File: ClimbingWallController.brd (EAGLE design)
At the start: 100 x 80 mm, 339 parts, among them IC1 74HCT138D, IC2 SN74LV4052AD, IC3 PIC24FJ32GB004, IC4 TLC5952, IC5 TLC5952, IC6 TC1015, IC8 74HCT138D, IC9 SN74LV4052AD, J1 PWR, Q1 DPBT8105, Q10 DPBT8105, Q11 DPBT8105, Q12 DPBT8105, Q13 DPBT8105, Q14 DPBT8105, Q15 DPBT8105, Q16 DPBT8105, Q17 DPBT8105, Q2 DPBT8105, Q3 DPBT8105, Q4 DPBT8105, Q5 DPBT8105, Q6 DPBT8105, Q7 DPBT8105, Q8 DPBT8105, Q9 NC, X1 MINI-USB-32005-201

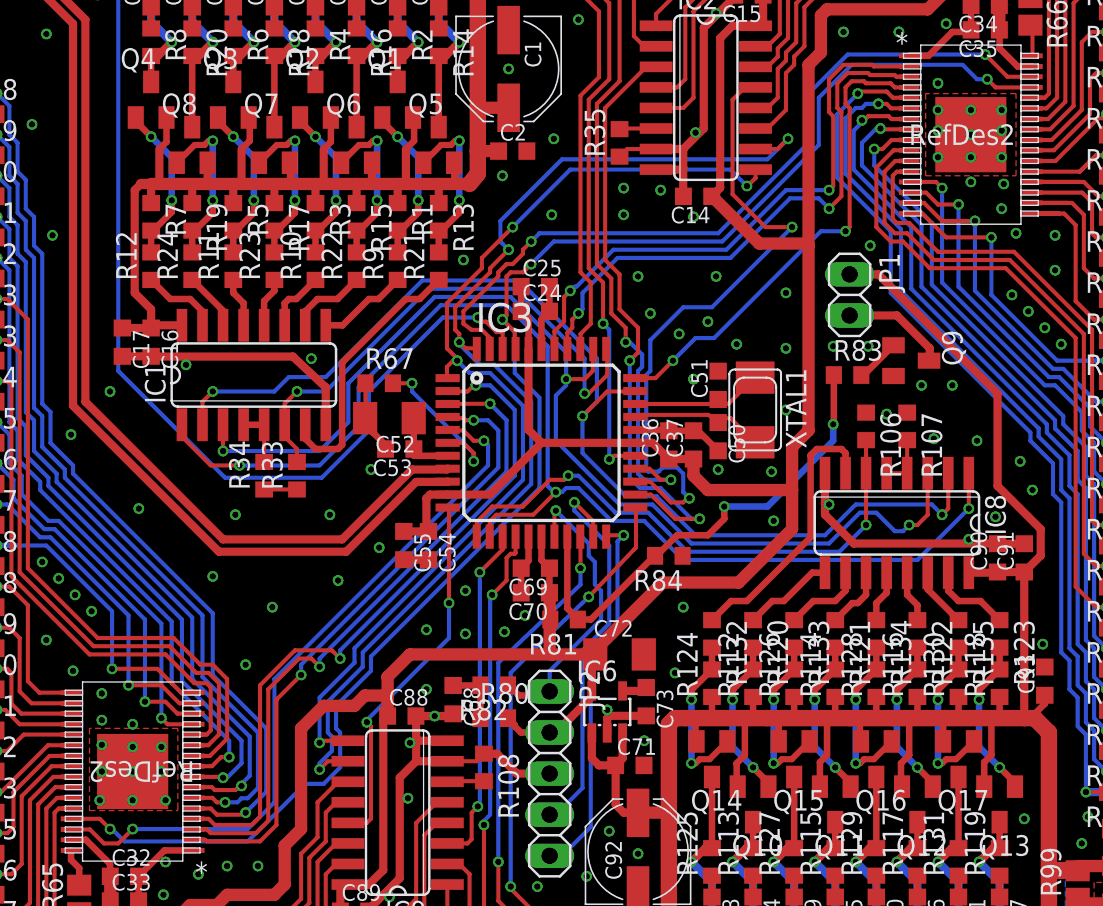
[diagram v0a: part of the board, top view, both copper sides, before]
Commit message: Optimized LED Driver footprint and paste mask to match the datasheet. Optimized a few signal routes to reduce noise coupling. Reviewed trace coupling on sensitive nodes. (Layout is good).
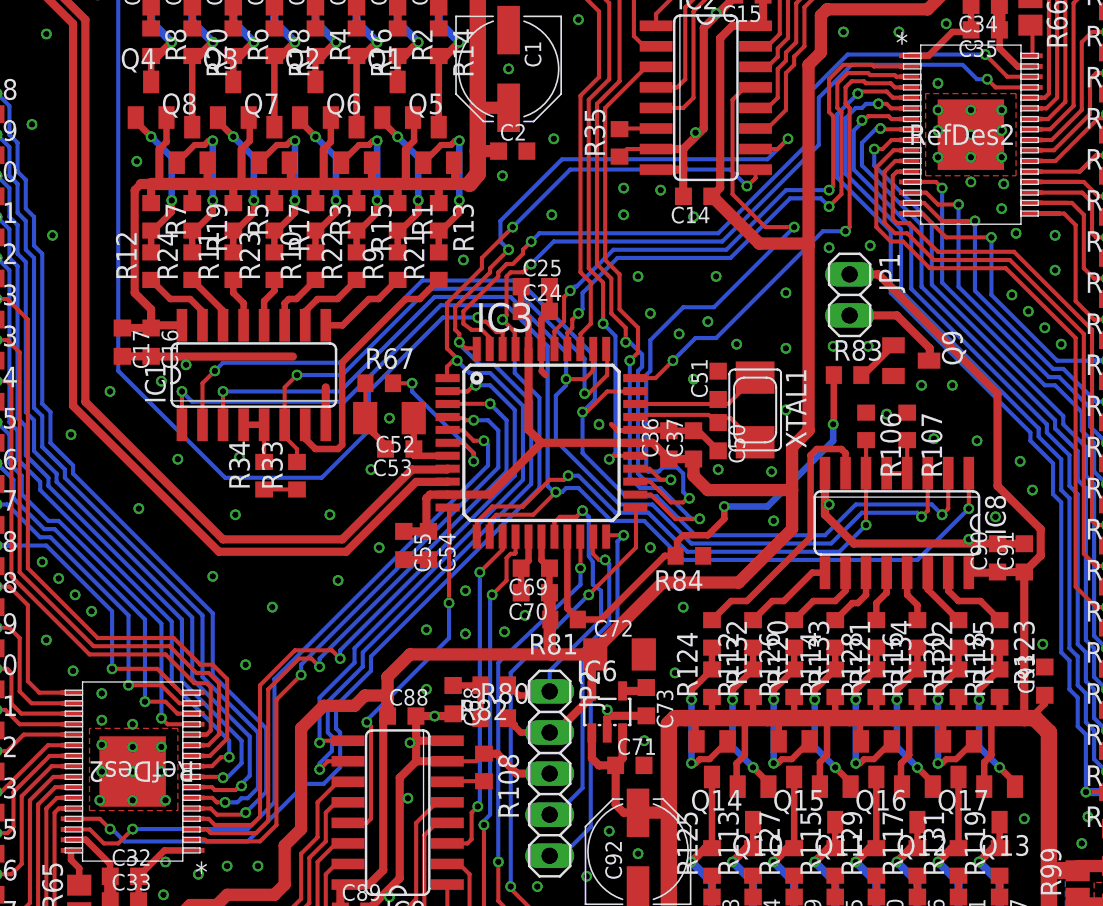
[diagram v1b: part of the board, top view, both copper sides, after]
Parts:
- moved R84 1.27 mm to (58.7, 33.7)
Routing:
- net PGED: track 24.6 -> 19.6 mm
- net RSEL2: track 69.0 -> 65.6 mm
- net RSEL0: track 76.7 -> 75.2 mm
- net MCLR_: track 18.2 -> 18.9 mm
- net RBEN: track 32.9 -> 33.4 mm
- net GND: track 345.3 -> 345.4 mm, vias 247 -> 254

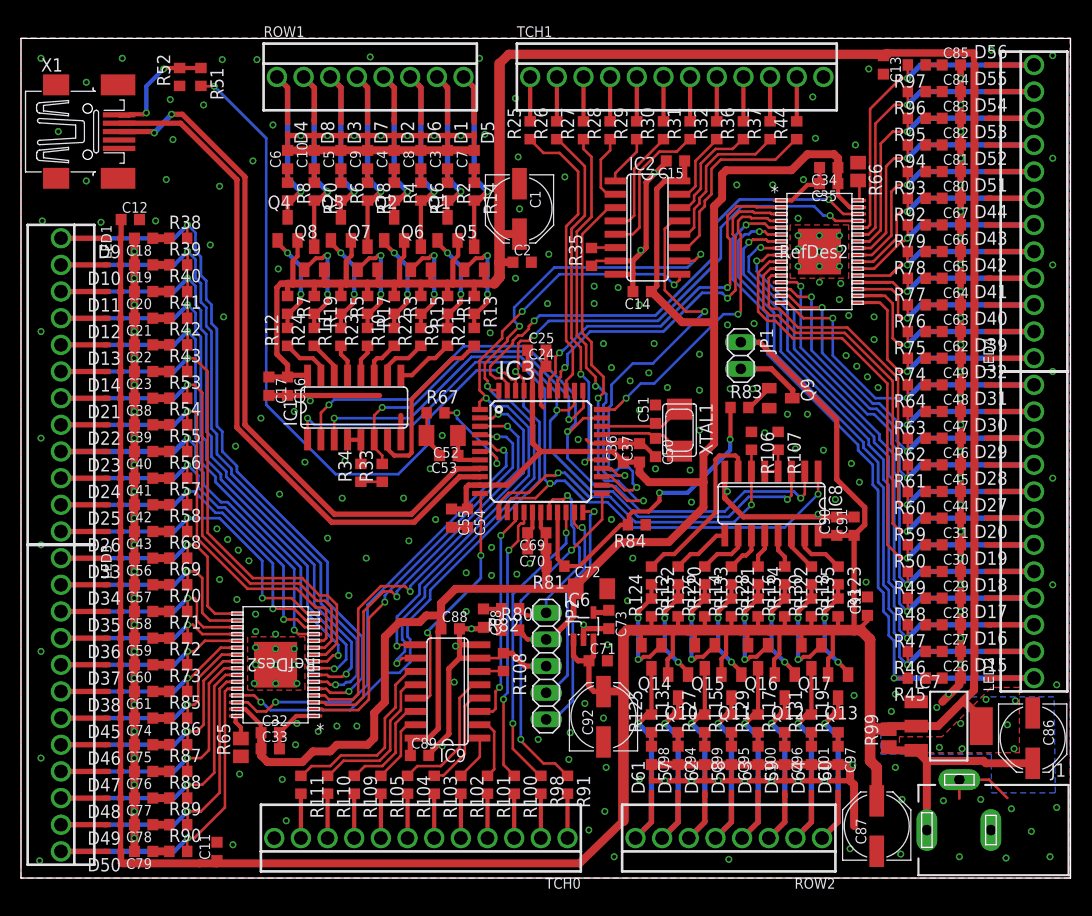
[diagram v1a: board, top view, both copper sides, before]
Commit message: Improved 5v power routing for etching concerns.
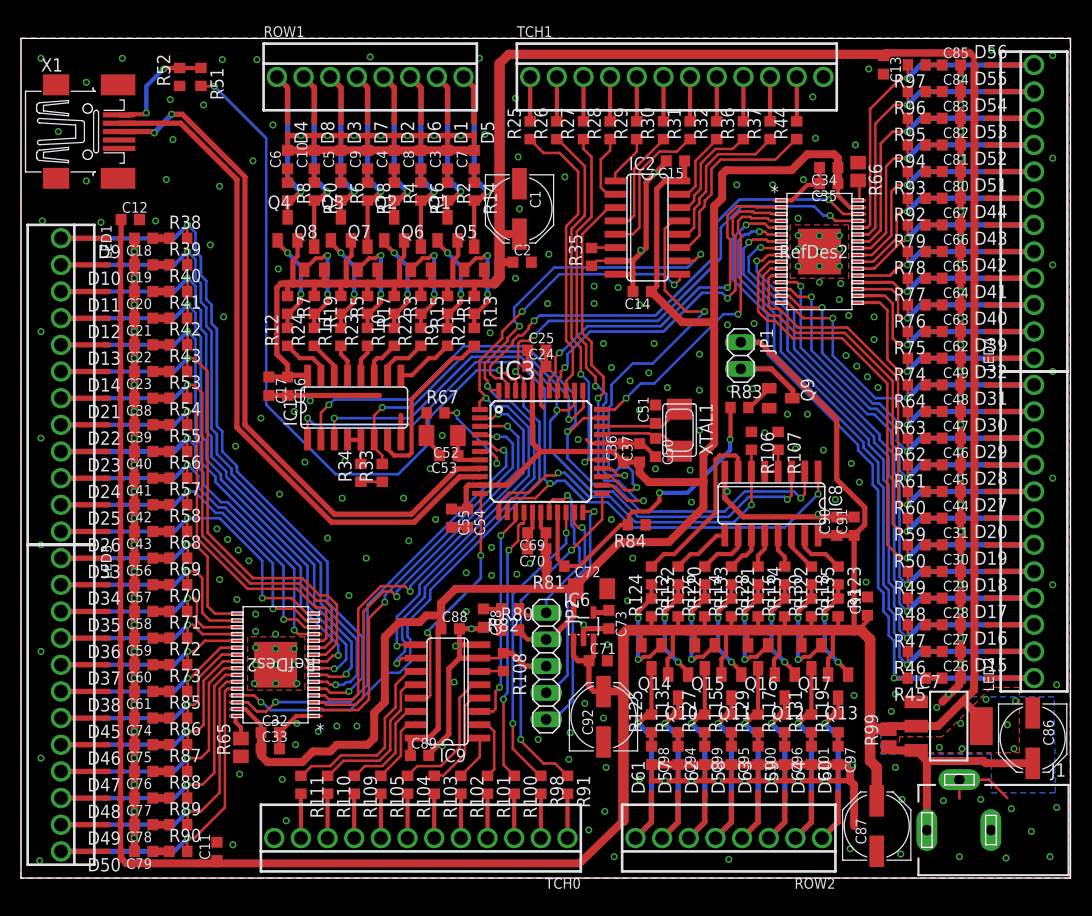
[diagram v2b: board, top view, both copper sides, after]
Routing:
- net +5V: track 491.3 -> 490.8 mm
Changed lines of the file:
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@@
 <setting verticaltext="up"/>
 </settings>
-<grid distance="0.05" unitdist="inch" unit="inch" style="lines" multiple="1" display="yes" altdistance="0.005" altunitdist="inch" altunit="inch"/>
+<grid distance="0.5" unitdist="mil" unit="mil" style="lines" multiple="1" display="yes" altdistance="0.005" altunitdist="inch" altunit="inch"/>
 <layers>
 <layer number="1" name="Top" color="4" fill="1" visible="yes" active="yes"/>
@@
 <layer number="25" name="tNames" color="7" fill="1" visible="yes" active="yes"/>
 <layer number="26" name="bNames" color="7" fill="1" visible="yes" active="yes"/>
-<layer number="27" name="tValues" color="7" fill="1" visible="no" active="yes"/>
-<layer number="28" name="bValues" color="7" fill="1" visible="no" active="yes"/>
+<layer number="27" name="tValues" color="7" fill="1" visible="yes" active="yes"/>
+<layer number="28" name="bValues" color="7" fill="1" visible="yes" active="yes"/>
 <layer number="29" name="tStop" color="7" fill="3" visible="yes" active="yes"/>
 <layer number="30" name="bStop" color="7" fill="6" visible="yes" active="yes"/>
@@
 <layer number="199" name="Contour" color="7" fill="1" visible="yes" active="yes"/>
 <layer number="200" name="200bmp" color="1" fill="10" visible="yes" active="yes"/>
-<layer number="201" name="201bmp" color="2" fill="1" visible="no" active="no"/>
-<layer number="202" name="202bmp" color="3" fill="1" visible="no" active="no"/>
+<layer number="201" name="201bmp" color="2" fill="10" visible="yes" active="yes"/>
+<layer number="202" name="202bmp" color="3" fill="10" visible="yes" active="yes"/>
 <layer number="203" name="203bmp" color="4" fill="10" visible="yes" active="yes"/>
 <layer number="204" name="204bmp" color="5" fill="10" visible="yes" active="yes"/>
@@
 <wire x1="57.404" y1="5.461" x2="53.213" y2="1.397" width="0.762" layer="1"/>
 <wire x1="53.213" y1="1.397" x2="17.018" y2="1.397" width="0.762" layer="1"/>
-<wire x1="17.018" y1="1.397" x2="9.652" y2="1.397" width="0.762" layer="1"/>
-<wire x1="9.652" y1="1.397" x2="9.525" y2="1.397" width="0.635" layer="1"/>
-<wire x1="9.525" y1="1.397" x2="9.525" y2="2.505" width="0.635" layer="1"/>
+<wire x1="17.018" y1="1.397" x2="10.033" y2="1.397" width="0.762" layer="1"/>
+<wire x1="10.033" y1="1.397" x2="9.525" y2="1.905" width="0.635" layer="1"/>
+<wire x1="9.525" y1="1.905" x2="9.525" y2="2.505" width="0.635" layer="1"/>
 <wire x1="9.525" y1="2.505" x2="9.49" y2="2.54" width="0.762" layer="1"/>
 <wire x1="27.305" y1="47.9044" x2="25.5664" y2="47.9044" width="0.508" layer="1"/>
@@
 <wire x1="24.384" y1="56.261" x2="24.765" y2="56.642" width="0.508" layer="1"/>
 <wire x1="24.765" y1="56.642" x2="25.4" y2="56.642" width="0.635" layer="1"/>
-<wire x1="90.805" y1="77.47" x2="90.805" y2="77.978" width="0.508" layer="1"/>
-<wire x1="90.805" y1="77.978" x2="90.805" y2="78.613" width="0.635" layer="1"/>
+<wire x1="90.805" y1="77.47" x2="90.805" y2="78.232" width="0.508" layer="1"/>
+<wire x1="90.805" y1="78.232" x2="90.424" y2="78.613" width="0.635" layer="1"/>
 <wire x1="82.55" y1="78.486" x2="46.482" y2="78.486" width="0.889" layer="1"/>
 <wire x1="46.482" y1="78.486" x2="45.593" y2="77.597" width="0.889" layer="1"/>
@@
 <wire x1="59.055" y1="23.368" x2="58.674" y2="23.368" width="0.4064" layer="1"/>
 <wire x1="82.169" y1="78.345" x2="82.536" y2="78.472" width="0.762" layer="1"/>
-<wire x1="90.805" y1="78.613" x2="82.55" y2="78.613" width="0.7112" layer="1"/>
+<wire x1="90.424" y1="78.613" x2="82.55" y2="78.613" width="0.7112" layer="1"/>
 <wire x1="82.55" y1="78.613" x2="82.31" y2="78.613" width="0.7112" layer="1"/>
 <wire x1="82.536" y1="78.472" x2="82.536" y2="78.599" width="0.254" layer="1"/>

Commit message: Added Logos to board. Cleaned up part names on board. Fixed LED driver part name.
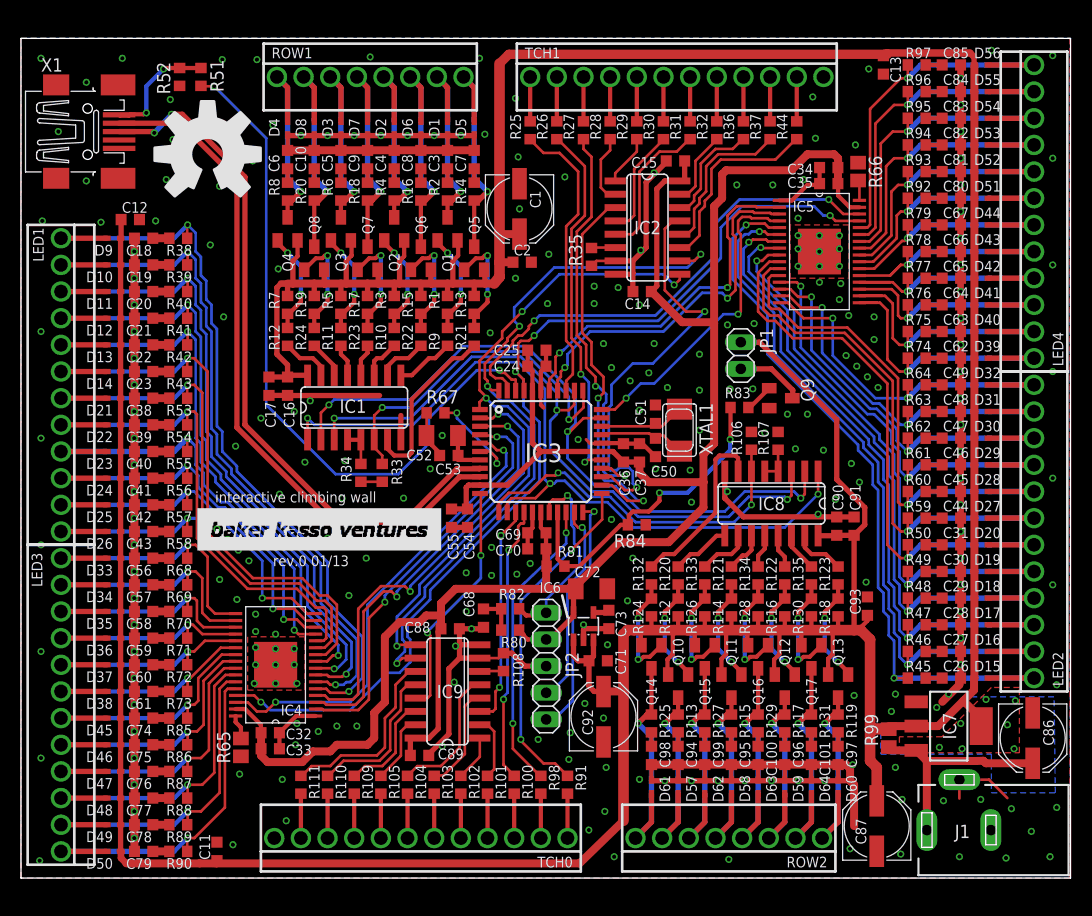
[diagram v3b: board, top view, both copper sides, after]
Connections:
- net C0_LAT: now also IC5.>VALUE; no longer IC5.4
- net C1_LAT: now also IC4.>VALUE; no longer IC4.4
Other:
- board text added: "/Users/matt/Downloads/bkventures_black.bmp"
- board text added: "interactive climbing wall"
- board text added: "rev.0 01/13"

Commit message: Updated NC status on column clamp diodes. Added new datasheet.
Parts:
- C11, C12, C13: value 0.1uF -> NC
- D10, D11, D12, D13, D14, D15, D16, D17, D18, D19, D20, D21, D22, D23, D24, D25, D26, D27, D28, D29, D30, D31, D32, D33, D34, D35, D36, D37, D38, D39, D40, D41, D42, D43, D44, D45, D46, D47, D48, D49, D50, D51, D52, D53, D54, D55, D56, D9: value RB521S30T1G -> NC
